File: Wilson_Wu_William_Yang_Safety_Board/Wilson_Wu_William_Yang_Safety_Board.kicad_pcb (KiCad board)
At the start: 2 copper layers, 122.4 x 168.1 mm, 115 parts, among them J1 22035035, J18 XT60-M, J2 22035035, J3 430450200, J4 M22-7130442, J5 430450200, J6 XT60-M, J7 XT60-M, J8 430450200, J9 Molex Micro-Fit 4 Pin, Q1 IRLML6344TRPBF, Q2 IRLML6344TRPBF, Q3 NTBLS0D8N08XTXG, Q4 NTBLS0D8N08XTXG, U1 STM32, U10 LTC4364HS, U11 LMV331IDBVR, U12 J115F11AH12VDCS61.5U, U13 ISOM8110DFGRQ1, U15 INA826AID, U16 J115F11AH12VDCS61.5U, U2 MCP2562-E_P, U3 10kohm, U4 SN74HCS21QPWRQ1, U5 J115F11AH12VDCS61.5U, U6 J115F11AH12VDCS61.5U, U7 LM1117IDTX-5.0/NOPB, U8 LM1117IMPX-ADJ/NOPB, U9 100 ohm

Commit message: update
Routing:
- net Net-(U10-DGATE): track 30.0 -> 0.00 mm, vias 3 -> 0
- net Net-(U10-SENSE): track 0.00 -> 11.2 mm, vias 0 -> 2
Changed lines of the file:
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@@
 	(gr_poly
 		(pts
-			(xy 88.5 30) (xy 88.75 29.75) (xy 88.5 29.75) (xy 88.5 29.75) (xy 88.5 32.8) (xy 90.832058 32.8)
-			(xy 92.702265 32.847735) (xy 93.65 32.829979) (xy 93.65 29.8) (xy 94 29.45) (xy 98.05 29.45) (xy 98.05 25)
-			(xy 97.75 24.7) (xy 96.25 24.5) (xy 95.25 23.5) (xy 95.25 18.75) (xy 94.75 18.25) (xy 89 18.25) (xy 88.5 18.75)
-			(xy 88.5 29.5) (xy 88.5 19)
+			(xy 88.5 29.5) (xy 88.75 29.75) (xy 88.8 29.75) (xy 88.8 32.8) (xy 90.832058 32.8) (xy 92.702265 32.847735)
+			(xy 93.65 32.829979) (xy 93.65 29.8) (xy 94 29.1) (xy 98.05 29.1) (xy 98.05 25) (xy 97.75 24.7) (xy 96.25 24.5)
+			(xy 95.25 23.5) (xy 95.25 18.75) (xy 94.75 18.25) (xy 89 18.25) (xy 88.5 18.75) (xy 88.5 29.5) (xy 88.5 19.3)
 		)
 		(stroke
@@
 	(gr_poly
 		(pts
-			(xy 107.5 44.1) (xy 107.5 45.2) (xy 108.3 45.2) (xy 109.8 43.7) (xy 109.8 41.3) (xy 109.7 41.2) (xy 108.6 41.2)
-			(xy 108.6 43)
+			(xy 107.648279 44.124761) (xy 107.689663 45.1) (xy 108.3 45.1) (xy 109.8 43.7) (xy 109.8 41.3) (xy 109.7 41.2)
+			(xy 108.6 41.2) (xy 108.6 43)
 		)
 		(stroke
@@
 	(gr_poly
 		(pts
-			(xy 87.25 37.0388) (xy 95.75 37.0388) (xy 95.75 38.75) (xy 100 38.75) (xy 104 34.75) (xy 104 30.75)
-			(xy 102.7 29.45) (xy 102.25 29.45) (xy 102.25 27) (xy 103.5 27) (xy 103.5 29.45) (xy 104.8 30.75)
-			(xy 105 30.75) (xy 105 40.5) (xy 105 38.75) (xy 106.75 40.5) (xy 106.75 43.5) (xy 107.25 44) (xy 107.25 47.25)
-			(xy 98.25 47.25) (xy 97.75 46.75) (xy 97.75 41.25) (xy 97.25 40.75) (xy 87.25 40.75) (xy 87.25 37.0388)
+			(xy 87.25 37.0388) (xy 95.55 37.2) (xy 95.55 38.75) (xy 100 38.75) (xy 104.2 34.55) (xy 104.2 30.95)
+			(xy 102.780486 29.4) (xy 102.7 29.4) (xy 102.7 27.3) (xy 103.5 27.3) (xy 103.5 29.45) (xy 104.8 30.75)
+			(xy 104.773778 31.362851) (xy 104.430952 39.375172) (xy 104.587563 38.767286) (xy 106.75 40.5) (xy 106.75 43.5)
+			(xy 107.05 43.8) (xy 107.05 47.05) (xy 98.05 47.05) (xy 97.75 46.75) (xy 97.75 41.25) (xy 97.25 40.75)
+			(xy 87.25 40.75) (xy 87.25 37.0388)
 		)
 		(stroke
@@
 	(gr_poly
 		(pts
-			(xy 93.75 33.75) (xy 93.75 36.5125) (xy 93.7125 36.55) (xy 86.5 36.55) (xy 86.5 41.5) (xy 97.5 41.5)
-			(xy 97.5 49.746601) (xy 97.355401 49.8912) (xy 84.5 49.8912) (xy 84.5 33.75)
+			(xy 92.85 33.75) (xy 92.85 36.6) (xy 92.65 36.55) (xy 86.5 36.55) (xy 86.5 41.5) (xy 97.1 41.5) (xy 97.1 49.7912)
+			(xy 97 49.8912) (xy 84.5 49.8912) (xy 84.5 33.75)
 		)
 		(stroke
@@
 	(gr_poly
 		(pts
-			(xy 119.75 34.75) (xy 124.5 34.75) (xy 126 36.25) (xy 126 40) (xy 118 40) (xy 117.75 39.75) (xy 117.75 39.25)
-			(xy 117.508 39.008) (xy 115.658205 39.008) (xy 115.658205 37.5) (xy 117.180205 37.5) (xy 117.5 37.180205)
+			(xy 101.3 29.7) (xy 101.3 30) (xy 100.039853 30.1) (xy 96.6 32.133047) (xy 96.6 36.8) (xy 96.1 37.3)
+			(xy 96.1 37.3) (xy 96.1 38.2) (xy 99.9 38.2) (xy 103.5 34.6) (xy 103.5 30.9) (xy 102.6 30) (xy 102 30)
+			(xy 102 27.3) (xy 101.9 27.2) (xy 101.3 27.2)
+		)
+		(stroke
+			(width 0.2)
+			(type solid)
+		)
+		(fill yes)
+		(layer "F.Cu")
+		(net 39)
+	)
+	(gr_poly
+		(pts
+			(xy 119.75 34.75) (xy 124.5 34.75) (xy 126 36.25) (xy 126 40) (xy 118.8 40) (xy 117.75 38.95) (xy 117.75 39)
+			(xy 117.508 39.008) (xy 115.658205 39.008) (xy 115.658205 37.6) (xy 117.080205 37.6) (xy 117.5 37.180205)
 			(xy 117.5 37)
 		)
@@
 	(gr_poly
 		(pts
-			(xy 119.75 34.75) (xy 124.5 34.75) (xy 126 36.25) (xy 126 40) (xy 118 40) (xy 117.75 39.75) (xy 117.75 39.25)
+			(xy 119.75 34.75) (xy 124.5 34.75) (xy 126 36.25) (xy 126 40) (xy 118.2 40) (xy 117.75 39.55) (xy 117.75 39.25)
 			(xy 117.508 39.008) (xy 115.658205 39.008) (xy 115.658205 37.5) (xy 117.180205 37.5) (xy 117.5 37.180205)
 			(xy 117.5 37)
@@
 	)
 	(segment
-		(start 116.499999 41.000001)
-		(end 115.500001 41.000001)
-		(width 0.5)
-		(layer "F.Cu")
-		(net 2)
-	)
-	(segment
 		(start 135.400001 35.9)
 		(end 135.400001 35.265002)
@@
 	)
 	(segment
+		(start 115.5 41)
+		(end 117.5 41)
+		(width 0.2)
+		(layer "F.Cu")
+		(net 2)
+	)
+	(segment
 		(start 35.05 117.7)
 		(end 35.05 118.8025)
@@
 	)
 	(segment
-		(start 117.5 40)
-		(end 116.499999 41.000001)
-		(width 0.5)
-		(layer "F.Cu")
-		(net 2)
-	)
-	(segment
 		(start 54.79 150.64)
 		(end 54.75 150.6)
@@
 	)
 	(via
-		(at 117.5 40)
-		(size 0.6)
-		(drill 0.3)
-		(layers "F.Cu" "B.Cu")
-		(net 2)
-	)
-	(via
 		(at 82.65 96.68)
 		(size 0.6)
@@
 	)
 	(via
+		(at 117.5 41)
+		(size 0.6)
+		(drill 0.3)
+		(layers "F.Cu" "B.Cu")
+		(net 2)
+	)
+	(via
 		(at 62.25 126.5)
 		(size 0.6)
@@
 	)
 	(segment
-		(start 96.45 34.55)
-		(end 97.342155 33.657845)
-		(width 0.85)
-		(layer "F.Cu")
-		(net 39)
-	)
-	(segment
-		(start 101.615 28.225)
-		(end 101.615 31.661)
-		(width 0.85)
-		(layer "F.Cu")
-		(net 39)
-	)
-	(segment
-		(start 101.615 31.661)
-		(end 100.5 32.776)
-		(width 0.85)
-		(layer "F.Cu")
-		(net 39)
-	)
-	(segment
-		(start 97.342155 33.657845)
-		(end 97.342155 33.342155)
-		(width 0.75)
-		(layer "F.Cu")
-		(net 39)
-	)
-	(segment
-		(start 96.45 37.75)
-		(end 96.45 34.55)
-		(width 0.85)
-		(layer "F.Cu")
-		(net 39)
-	)
-	(segment
-		(start 97.342155 33.342155)
-		(end 94.5 30.5)
-		(width 0.75)
-		(layer "F.Cu")
-		(net 39)
-	)
-	(segment
-		(start 97.75 33.25)
-		(end 100.026 33.25)
-		(width 6.75)
-		(layer "F.Cu")
-		(net 39)
-	)
-	(segment
-		(start 100.026 33.25)
-		(end 100.5 32.776)
-		(width 6.75)
-		(layer "F.Cu")
-		(net 39)
-	)
-	(segment
-		(start 97.342155 33.657845)
-		(end 97.342155 36.592155)
-		(width 0.75)
-		(layer "F.Cu")
-		(net 39)
-	)
-	(segment
-		(start 97.342155 36.592155)
-		(end 98.25 37.5)
-		(width 0.75)
-		(layer "F.Cu")
-		(net 39)
-	)
-	(segment
-		(start 100.5 37)
-		(end 100 37.5)
-		(width 0.75)
-		(layer "F.Cu")
-		(net 39)
-	)
-	(segment
-		(start 100.5 32.776)
-		(end 100.5 37)
-		(width 0.75)
-		(layer "F.Cu")
-		(net 39)
-	)
-	(segment
-		(start 97.75 33.25)
-		(end 97.342155 33.657845)
-		(width 6.75)
-		(layer "F.Cu")
-		(net 39)
-	)
-	(via
-		(at 94.5 30.5)
-		(size 0.6)
-		(drill 0.3)
-		(layers "F.Cu" "B.Cu")
-		(net 39)
-	)
-	(via
-		(at 100 37.5)
-		(size 0.6)
-		(drill 0.3)
-		(layers "F.Cu" "B.Cu")
-		(net 39)
-	)
-	(via
-		(at 98.25 37.5)
-		(size 0.6)
-		(drill 0.3)
-		(layers "F.Cu" "B.Cu")
-		(net 39)
-	)
-	(segment
-		(start 100.026 33.224)
-		(end 100.5 32.75)
-		(width 6.75)
-		(layer "B.Cu")
-		(net 39)
-	)
-	(segment
-		(start 97.75 33.224)
-		(end 100.026 33.224)
-		(width 6.75)
-		(layer "B.Cu")
-		(net 39)
-	)
-	(segment
-		(start 97.75 33.224)
-		(end 97.342155 33.631845)
-		(width 6.75)
-		(layer "B.Cu")
-		(net 39)
-	)
-	(segment
 		(start 86.097799 32.25)
 		(end 87.772201 32.25)
@@
 	)
 	(segment
+		(start 98.159069 30.01765)
+		(end 98.017649 30.01765)
+		(width 0.85)
+		(layer "F.Cu")
+		(net 108)
+	)
+	(segment
+		(start 92.18 35.1)
+		(end 92 35.28)
+		(width 0.85)
+		(layer "F.Cu")
+		(net 108)
+	)
+	(segment
+		(start 94.1 35.1)
+		(end 92.18 35.1)
+		(width 0.85)
+		(layer "F.Cu")
+		(net 108)
+	)
+	(segment
+		(start 99.075 29.101719)
+		(end 98.159069 30.01765)
+		(width 0.85)
+		(layer "F.Cu")
+		(net 108)
+	)
+	(segment
+		(start 99.075 28.225)
+		(end 99.075 29.101719)
+		(width 0.85)
+		(layer "F.Cu")
+		(net 108)
+	)
+	(via
+		(at 94.1 35.1)
+		(size 0.6)
+		(drill 0.3)
+		(layers "F.Cu" "B.Cu")
+		(net 108)
+	)
+	(via
+		(at 98.017649 30.01765)
+		(size 0.6)
+		(drill 0.3)
+		(layers "F.Cu" "B.Cu")
+		(net 108)
+	)
+	(segment
+		(start 98.017649 31.182351)
+		(end 94.1 35.1)
+		(width 6.75)
+		(layer "B.Cu")
+		(net 108)
+	)
+	(segment
+		(start 98.017649 30.01765)
+		(end 98.017649 31.182351)
+		(width 6.75)
+		(layer "B.Cu")
+		(net 108)
+	)
+	(segment

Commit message: layout
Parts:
- removed TP12: TestPoint, TestPoint:TestPoint_Pad_D1.0mm
- added ADJ_LDO_TP1: V_DIVIDED, TestPoint:TestPoint_Pad_D1.0mm, F.Cu at (38.7, 124.2)
- added load_neg_tp1: V_DIVIDED, TestPoint:TestPoint_Pad_D1.0mm, F.Cu at (80.8, 31.1)
- added load_switch_tp1: V_DIVIDED, TestPoint:TestPoint_Pad_D1.0mm, F.Cu at (119.9, 45.1)
- added load_switch_tp3: V_DIVIDED, TestPoint:TestPoint_Pad_D1.0mm, F.Cu at (101.5, 40.4)
- added mosfet_drain_tp1: V_DIVIDED, TestPoint:TestPoint_Pad_D1.0mm, F.Cu at (85.4, 93.8)
- added mosfet_drain_tp2: V_DIVIDED, TestPoint:TestPoint_Pad_D1.0mm, F.Cu at (80.2, 51.0)
- added octocoupler_tp1: V_DIVIDED, TestPoint:TestPoint_Pad_D1.0mm, F.Cu at (76.7, 102.6)
- added source_pos_tp1: V_DIVIDED, TestPoint:TestPoint_Pad_D1.0mm, F.Cu at (44.9, 40.6)
- added source_pos_tp2: V_DIVIDED, TestPoint:TestPoint_Pad_D1.0mm, F.Cu at (31.1, 80.0)
- TP17: value TestPoint -> 5V0_LDO_TP
- moved H1 2.60 mm to (30.1, 161.2)
- moved H4 2.60 mm to (143.3, 161.2)
- renumbered TP33 to CAN_NEG_TP1, TP32 to CAN_POS_TP1, TP8 to ESTOP_TP1, TP_48V6 to HFC_NEG_TP1, TP_48V5 to HFC_RELAY_TP1, TP10 to IgnitionSignal_TP1, TP4 to RELAY_O_TP1, TP15 to RXD_TP1, TP14 to TXD_TP1, TP16 to h_ref_tp1, TP9 to hsensor_output_tp1, TP13 to load_pos_tp1, TP1 to mosfet_conn_tp1, TP3 to new_hsensor_output_tp1, TP31 to old_hsensor_tp1
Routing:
- net load switch conn: track 59.0 -> 4.77 mm, vias 1 -> 108
- net Net-(D2-A): track 55.1 -> 65.7 mm
- net GND: track 55.1 -> 57.1 mm, vias 36 -> 153
- net Net-(U10-SENSE): track 11.2 -> 11.1 mm, vias 2 -> 0
- net load conn: vias 0 -> 42
- net Net-(U10-DGATE): vias 0 -> 21
- net /h-rensor relays/source_conn: vias 0 -> 51
- net /h-rensor relays/source negative: vias 0 -> 73
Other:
- board text removed: "LTC4364HS"

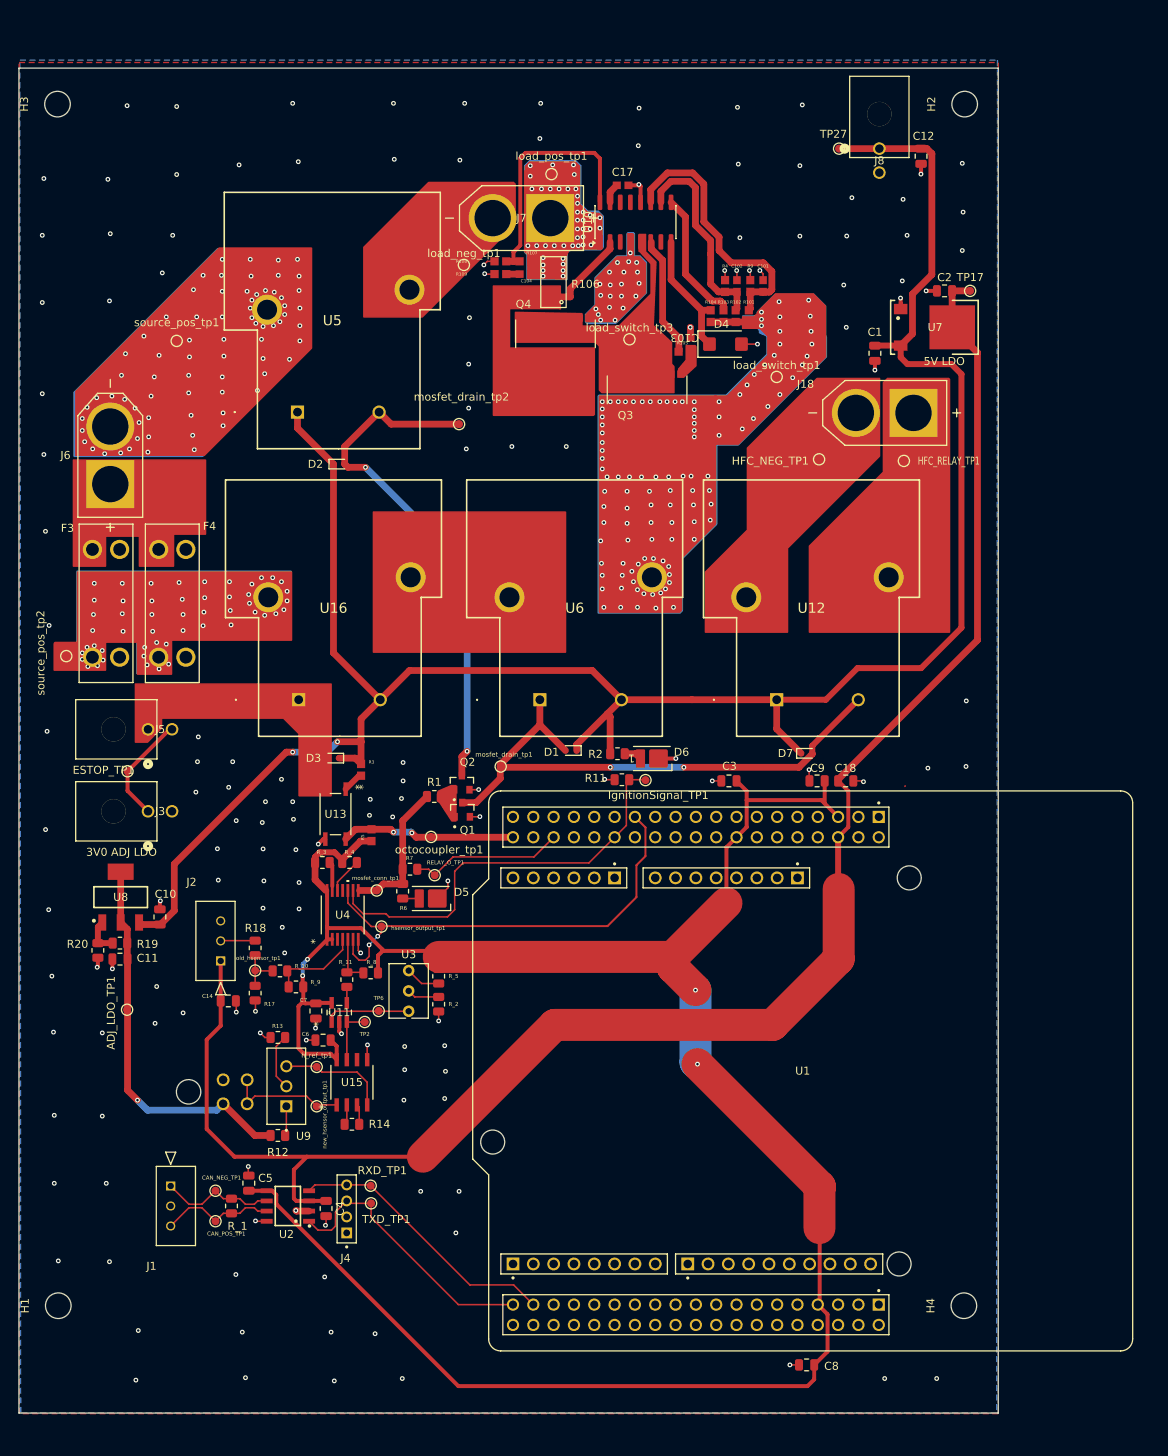
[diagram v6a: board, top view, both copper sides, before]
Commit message: layout fixes
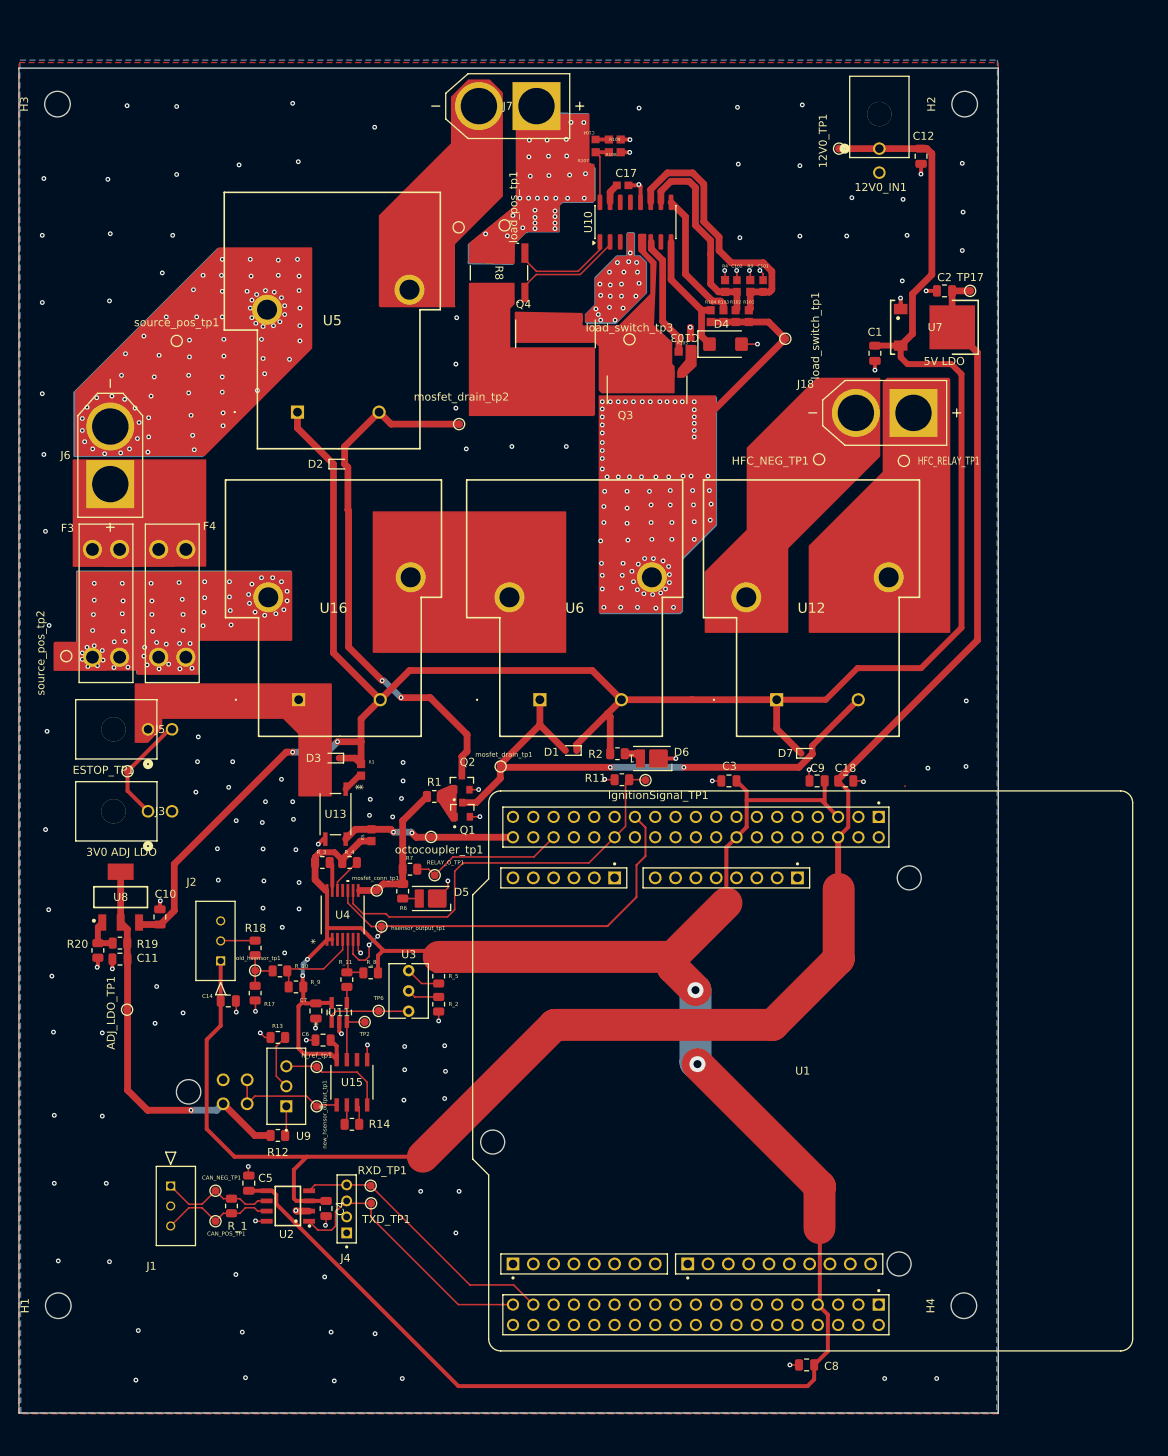
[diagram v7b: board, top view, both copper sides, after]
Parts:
- removed R106: 1.2m, Library:niche1.5ohmresistor
- added R8: WSLP27261L300FEA, 1.3ohmshunt:WSLP2726_1.3mOHM_VIS, F.Cu at (85.2, 32.1)
- R105: value R_US -> 10 ohm
- moved R109 22.1 mm to (99.7, 15.4), turned to 0 degrees
- moved R108 19.8 mm to (99.7, 17.0), turned to 0 degrees
- moved C104 18.6 mm to (96.5, 15.4), turned to 0 degrees
- moved R107 15.8 mm to (96.5, 17.0), turned to 0 degrees
- moved J7 14.1 mm to (86.3, 11.2)
- moved load_pos_tp1 8.68 mm to (85.9, 26.2), turned to 90 degrees
- moved load_switch_tp1 4.89 mm to (121.0, 40.3)
- moved load_neg_tp1 4.74 mm to (80.2, 26.4)
- renumbered J8 to 12V0_IN1, TP27 to 12V0_TP1
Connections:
- F3 pad 1_2: (no net) -> /h-rensor relays/source_conn
- F3 pad 2_2: (no net) -> Net-(J6-POS)
- F4 pad 1_2: (no net) -> /h-rensor relays/source_conn
- F4 pad 2_2: (no net) -> Net-(J6-POS)
- Q4 pad 9: Net-(U10-SENSE) -> Net-(Q4-Pad9)
- U10 pad 1: load conn -> Net-(U10-OUT)
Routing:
- net load switch conn: track 4.77 -> 32.6 mm, vias 108 -> 82
- net Net-(U10-FB): track 30.9 -> 8.14 mm
- net Net-(U10-OUT): track 0.00 -> 12.9 mm
- net Net-(U10-SENSE): track 11.1 -> 14.0 mm
- net Net-(D2-A): track 65.7 -> 66.7 mm
- net GND: track 57.1 -> 56.7 mm, vias 153 -> 145
- net load conn: vias 42 -> 31
- net /h-rensor relays/source_conn: vias 51 -> 59

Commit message: update
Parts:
- added Q5: IRLML6344TRPBF, Test:TRANS_IRLML6344TRPBF, F.Cu at (87.9, 93.7)
- added R_6: 0, Resistor_SMD:R_0805_2012Metric, F.Cu at (94.4, 93.7)
- added R_7: 0, Resistor_SMD:R_0805_2012Metric, F.Cu at (90.5, 94.7)
- moved mosfet_drain_tp1 1.80 mm to (83.6, 93.8)
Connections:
- D1 pad 2: /h-rensor relays/DRAIN -> Net-(D1-A)
- D7 pad 2: /h-rensor relays/DRAIN -> drain
- Q1 pad 3: /h-rensor relays/DRAIN -> Net-(D1-A)
- U1 pad 35: unconnected-(U1-PC2-Pad35) -> Net-(U1-PC2)
- U12 pad 2: /h-rensor relays/DRAIN -> drain
- U6 pad 1: /h-rensor relays/DRAIN -> Net-(D1-A)
- mosfet_drain_tp1 pad 1: /h-rensor relays/DRAIN -> Net-(D1-A)
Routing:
- net /h-rensor relays/DRAIN: track 71.4 -> 0.00 mm, vias 2 -> 0
- net drain: track 0.00 -> 46.9 mm, vias 0 -> 2
- net Net-(D1-A): track 0.00 -> 26.7 mm
- net Net-(U1-PC2): track 0.00 -> 9.95 mm
- net Net-(Q5-Pad3): track 0.00 -> 1.75 mm
- net GND: track 56.7 -> 57.9 mm, vias 145 -> 146
